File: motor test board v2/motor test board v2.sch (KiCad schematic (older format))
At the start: 8 parts, among them J1 Conn_01x02, J2 Conn_01x07, J3 Conn_01x02, U1 MC33887

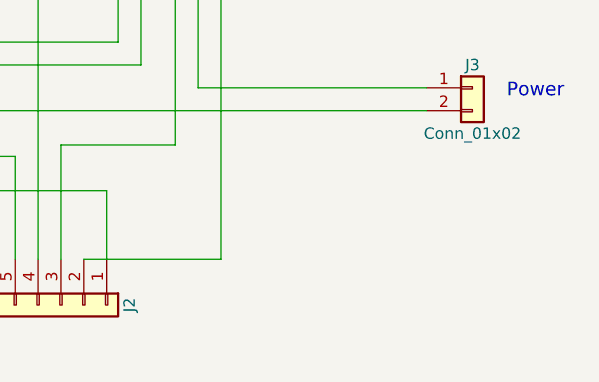
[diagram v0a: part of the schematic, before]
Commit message: added text to pcb
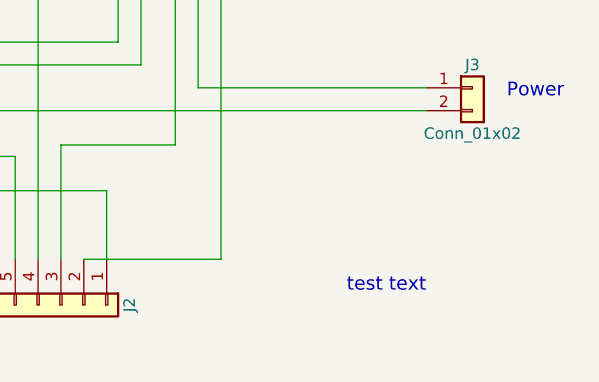
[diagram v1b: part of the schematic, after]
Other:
- note added: "test text"
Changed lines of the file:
@@
 LIBS:contrib
 LIBS:valves
-LIBS:motor test board-cache
 LIBS:motor test board v2-cache
 EELAYER 25 0
@@
 Text Notes 8100 4900 0    60   ~ 0
 Power\n
+Text Notes 7400 5750 0    60   ~ 0
+test text
 $EndSCHEMATC

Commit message: removed text
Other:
- note removed: "test text"
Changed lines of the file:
@@
 LIBS:contrib
 LIBS:valves
+LIBS:motor test board-cache
 LIBS:motor test board v2-cache
 EELAYER 25 0
@@
 Text Notes 8100 4900 0    60   ~ 0
 Power\n
-Text Notes 7400 5750 0    60   ~ 0
-test text
 $EndSCHEMATC
